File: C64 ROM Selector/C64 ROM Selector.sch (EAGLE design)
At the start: 6 parts, among them IC2 27256

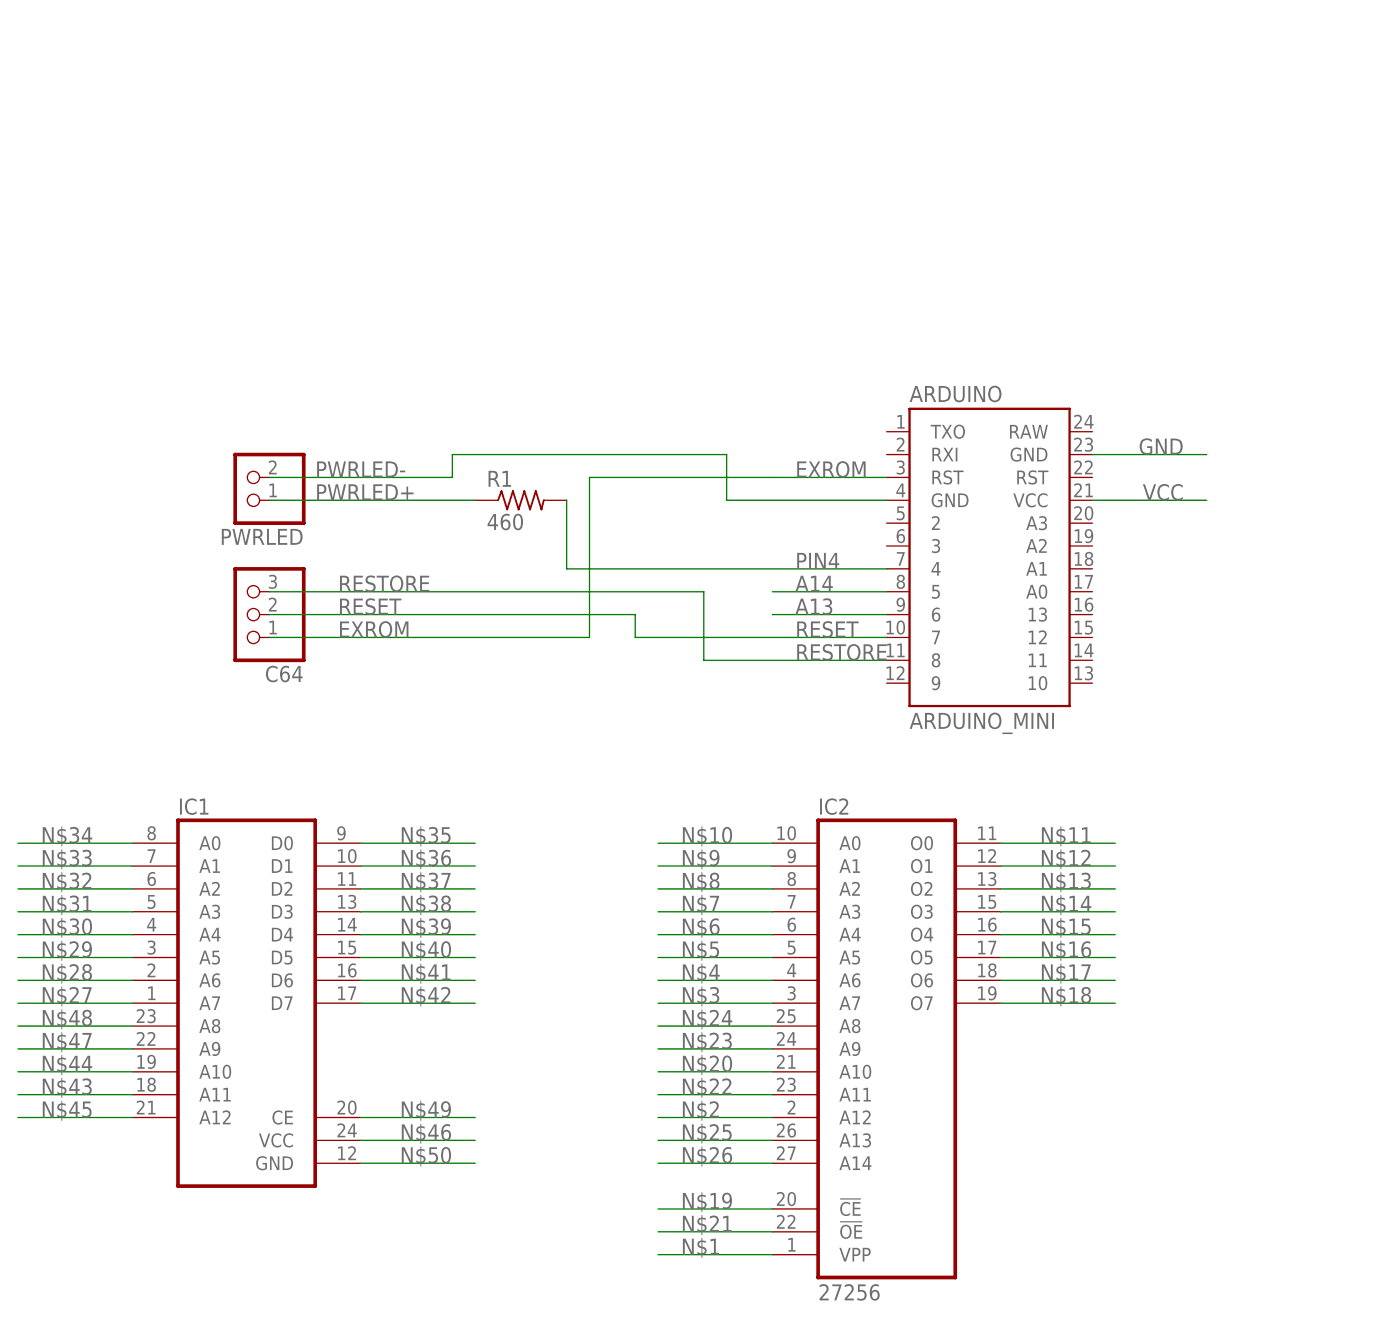
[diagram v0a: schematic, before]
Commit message: Finished C64 Rom Selector
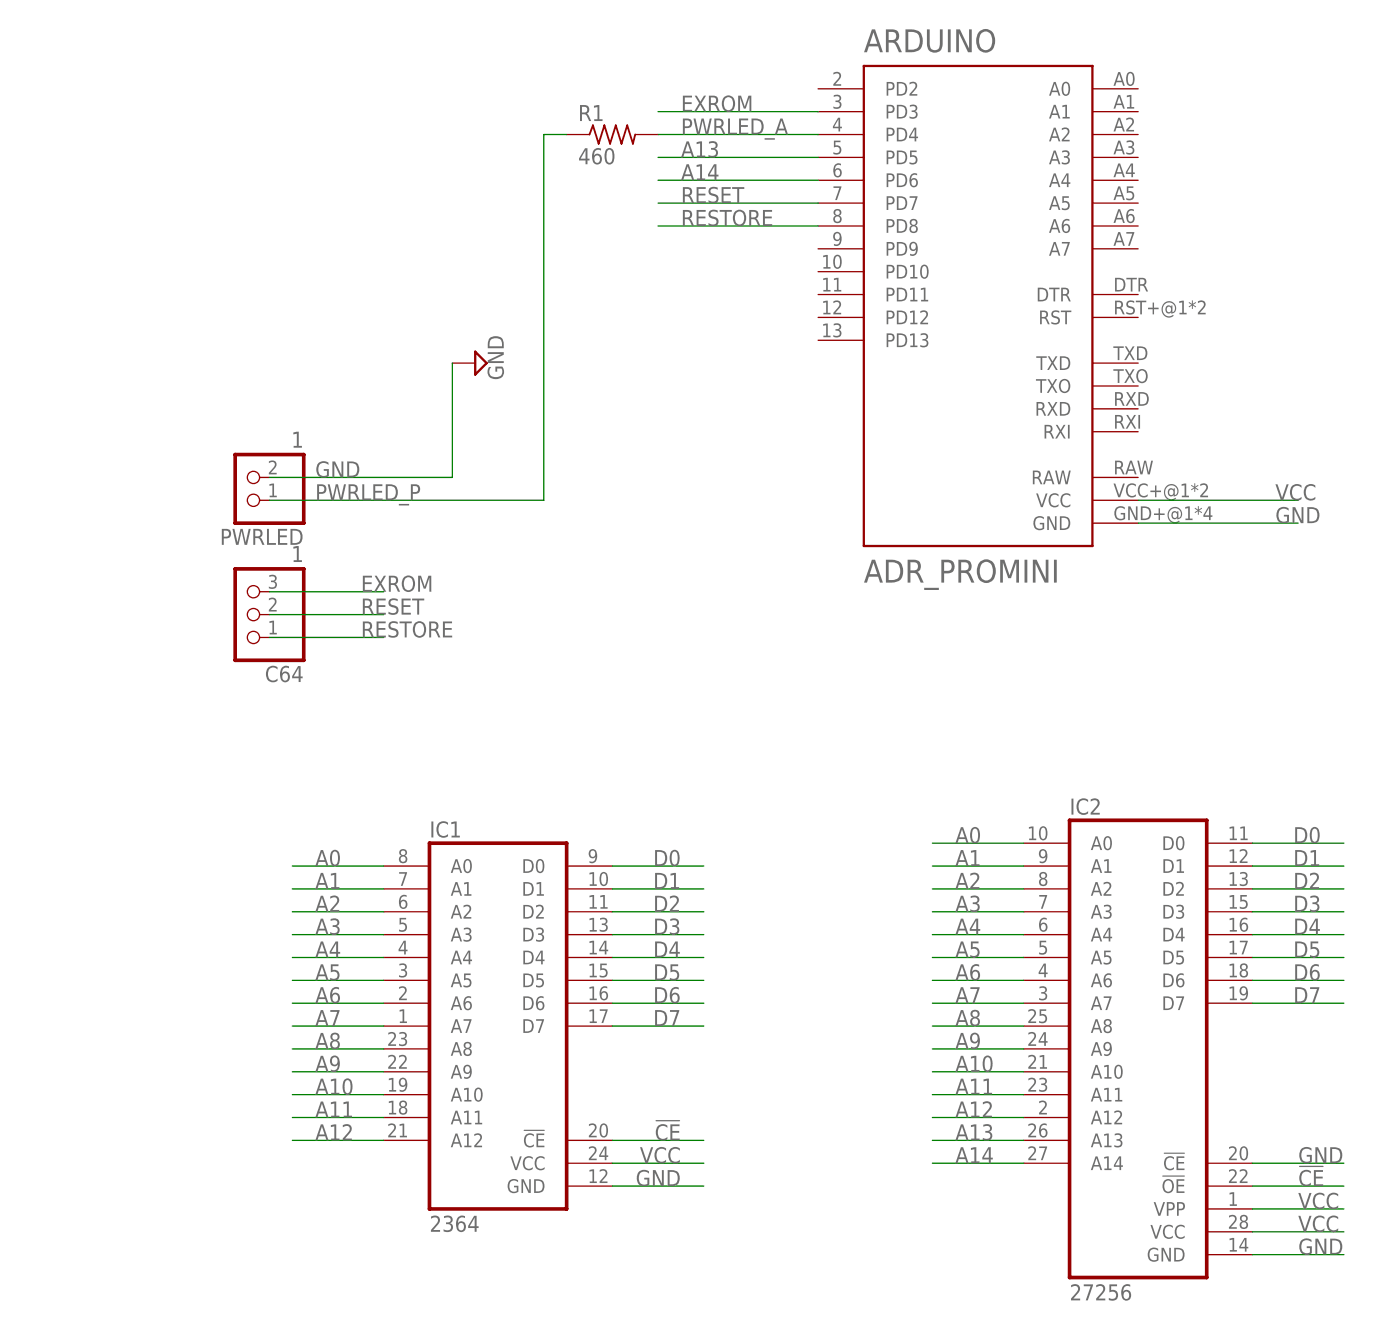
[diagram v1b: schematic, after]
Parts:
- ARDUINO: value ARDUINO_MINI -> ADR_PROMINI; device SparkFun-Retired:ARDUINO_MINI -> myparts:ADR_PROMINI
- C64, PWRLED: value (none) -> 1
- IC1: value (none) -> 2364; device 2364:2716 -> myparts:2364
- IC2: device memory:27256 -> myparts:27256
- R1: device rcl:R-US_0207/10 -> rcl:R-US_0204/7
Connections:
- net PWRLED+ renamed PWRLED_P
- removed net N$1: IC2A.VPP
- removed net N$10: IC2A.A0
- removed net N$11: IC2A.O0
- removed net N$12: IC2A.O1
- removed net N$13: IC2A.O2
- removed net N$14: IC2A.O3
- removed net N$15: IC2A.O4
- removed net N$16: IC2A.O5
- removed net N$17: IC2A.O6
- removed net N$18: IC2A.O7
- removed net N$19: IC2A.!CE
- removed net N$2: IC2A.A12
- removed net N$20: IC2A.A10
- removed net N$21: IC2A.!OE
- removed net N$22: IC2A.A11
- removed net N$23: IC2A.A9
- removed net N$24: IC2A.A8
- removed net N$25: IC2A.A13
- removed net N$26: IC2A.A14
- removed net N$27: IC1.A7
- removed net N$28: IC1.A6
- removed net N$29: IC1.A5
- removed net N$3: IC2A.A7
- removed net N$30: IC1.A4
- removed net N$31: IC1.A3
- removed net N$32: IC1.A2
- removed net N$33: IC1.A1
- removed net N$34: IC1.A0
- removed net N$35: IC1.D0
- removed net N$36: IC1.D1
- removed net N$37: IC1.D2
- removed net N$38: IC1.D3
- removed net N$39: IC1.D4
- removed net N$4: IC2A.A6
- removed net N$40: IC1.D5
- removed net N$41: IC1.D6
- removed net N$42: IC1.D7
- removed net N$43: IC1.A11
- removed net N$44: IC1.A10
- removed net N$45: IC1.A12
- removed net N$46: IC1.VCC
- removed net N$47: IC1.A9
- removed net N$48: IC1.A8
- removed net N$49: IC1.CE
- removed net N$5: IC2A.A5
- removed net N$50: IC1.GND
- removed net N$6: IC2A.A4
- removed net N$7: IC2A.A3
- removed net N$8: IC2A.A2
- removed net N$9: IC2A.A1
- removed net PIN4: ARDUINO.4, R1.2
- removed net PWRLED-: ARDUINO.GND, PWRLED.2
- new net !CE: IC1.!CE, IC2.!OE
- new net A0: IC1.A0, IC2.A0
- new net A1: IC1.A1, IC2.A1
- new net A10: IC1.A10, IC2.A10
- new net A11: IC1.A11, IC2.A11
- new net A12: IC1.A12, IC2.A12
- new net A2: IC1.A2, IC2.A2
- new net A3: IC1.A3, IC2.A3
- new net A4: IC1.A4, IC2.A4
- new net A5: IC1.A5, IC2.A5
- new net A6: IC1.A6, IC2.A6
- new net A7: IC1.A7, IC2.A7
- new net A8: IC1.A8, IC2.A8
- new net A9: IC1.A9, IC2.A9
- new net D0: IC1.D0, IC2.D0
- new net D1: IC1.D1, IC2.D1
- new net D2: IC1.D2, IC2.D2
- new net D3: IC1.D3, IC2.D3
- new net D4: IC1.D4, IC2.D4
- new net D5: IC1.D5, IC2.D5
- new net D6: IC1.D6, IC2.D6
- new net D7: IC1.D7, IC2.D7
- new net PWRLED_A: ARDUINO.PD4, R1.2
- net A13: now also ARDUINO.PD5, IC2.A13; no longer ARDUINO.6
- net A14: now also ARDUINO.PD6, IC2.A14; no longer ARDUINO.5
- net EXROM: now also ARDUINO.PD3, C64.3; no longer ARDUINO.RST, C64.1
- net GND: now also ARDUINO.GND, IC1.GND, IC2.!CE, IC2.GND, PWRLED.2; no longer ARDUINO.GND@2
- net RESET: now also ARDUINO.PD7; no longer ARDUINO.7
- net RESTORE: now also ARDUINO.PD8, C64.1; no longer ARDUINO.8, C64.3
- net VCC: now also IC1.VCC, IC2.VCC, IC2.VPP
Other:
- moved on the sheet: R1

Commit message: Minor edits to labels
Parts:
- IC1: value 2364 -> C64 ROM SOCKET
- IC2: value 27256 -> 27256 EEPROM
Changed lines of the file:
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@@
 <part name="SUPPLY1" library="supply2" library_urn="urn:adsk.eagle:library:372" deviceset="GND" device=""/>
 <part name="R1" library="rcl" library_urn="urn:adsk.eagle:library:334" deviceset="R-US_" device="0204/7" package3d_urn="urn:adsk.eagle:package:23498/2" value="460"/>
-<part name="IC1" library="myparts" deviceset="2364" device="" package3d_urn="urn:adsk.eagle:package:19955/2" value="2364"/>
-<part name="IC2" library="myparts" deviceset="27256" device="" package3d_urn="urn:adsk.eagle:package:31069/1" value="27256"/>
+<part name="IC1" library="myparts" deviceset="2364" device="" package3d_urn="urn:adsk.eagle:package:19955/2" value="C64 ROM SOCKET"/>
+<part name="IC2" library="myparts" deviceset="27256" device="" package3d_urn="urn:adsk.eagle:package:31069/1" value="27256 EEPROM"/>
 </parts>
 <sheets>
